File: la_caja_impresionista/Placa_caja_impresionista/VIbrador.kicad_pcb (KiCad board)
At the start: 2 copper layers, 8 parts, among them U1 Pila3,7V, U2 StepDown, U3 Buzzer, U4 HC-05, U5 Buzzer, U6 PiZeroW, U7 Pila3,7V-Modulos-VIbrador-res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

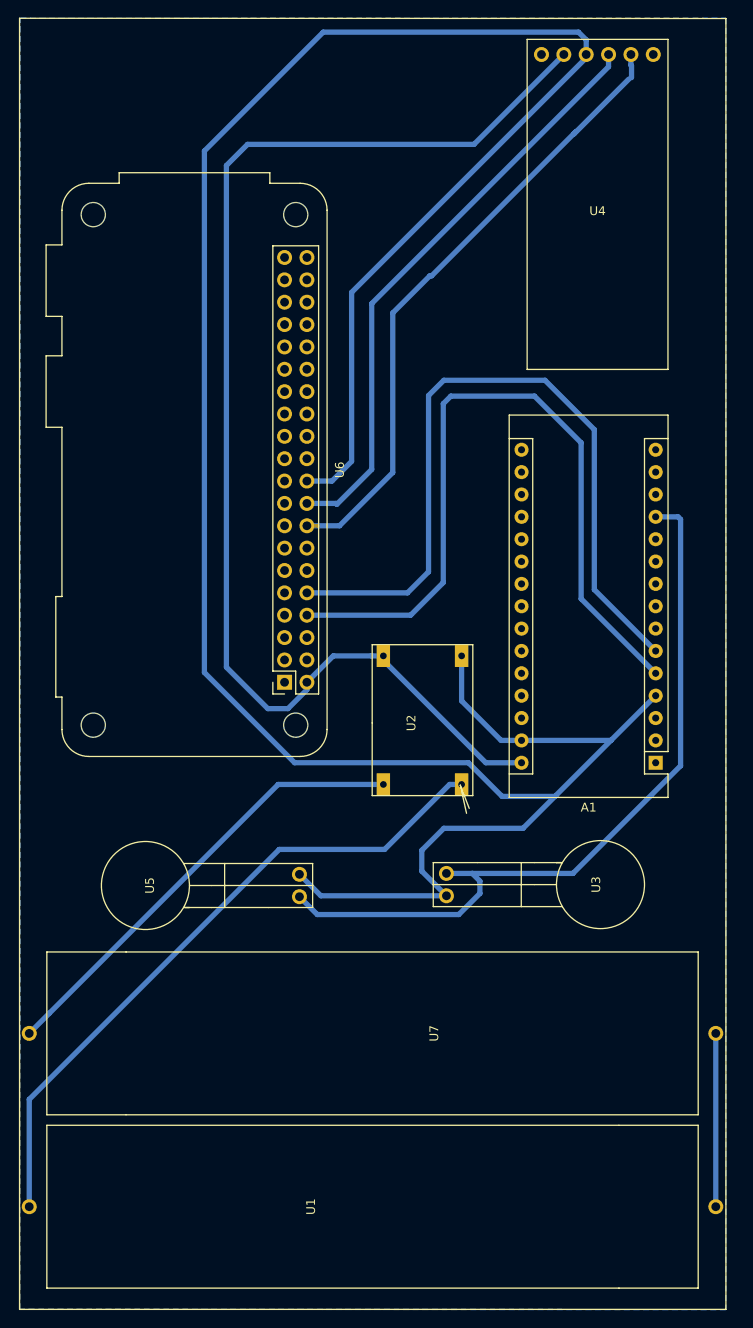
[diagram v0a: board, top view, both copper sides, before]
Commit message: Conexiones PCB
Quedo conectado todo feo y como el orto pero esta conectado que es mejor que nada despues hay que revisar todas las conexiones y dejarlas facheras
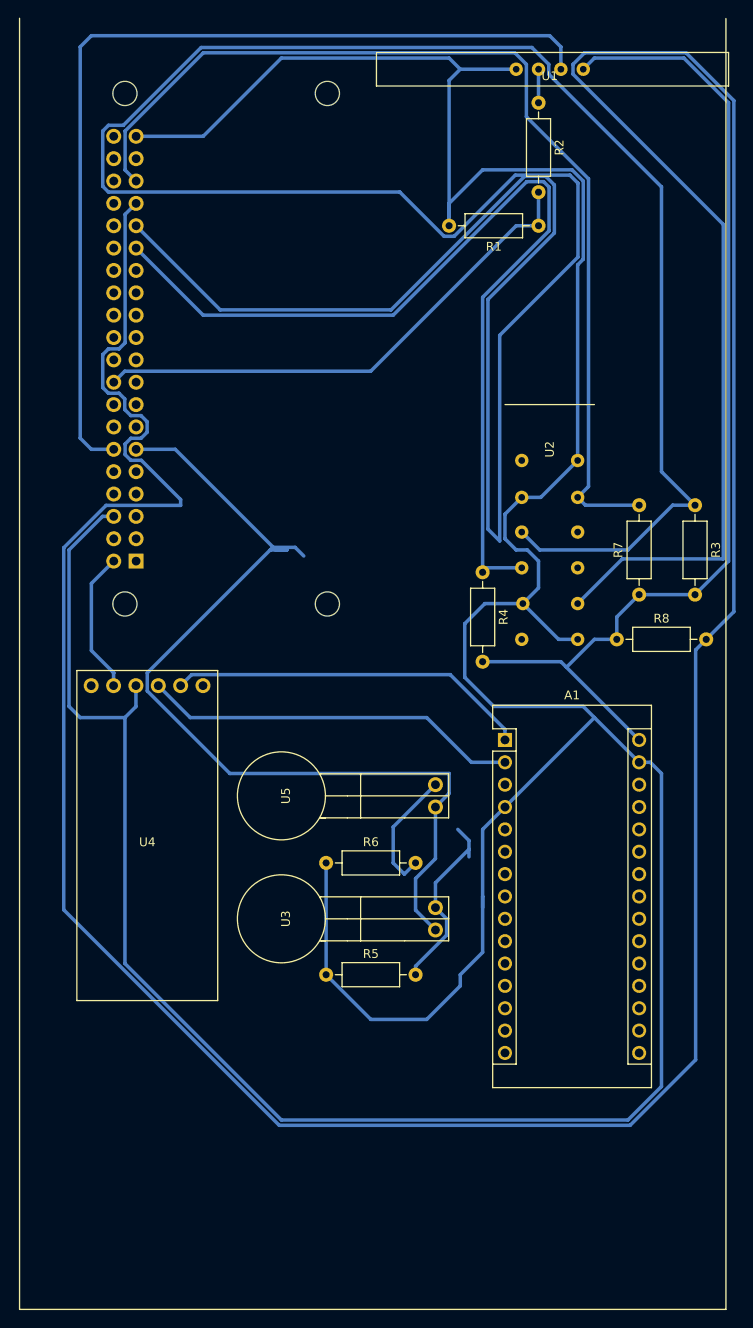
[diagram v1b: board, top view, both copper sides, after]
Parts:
- removed U7: Pila3,7V-Modulos-VIbrador-rescue, VibradorPCB:Pila de Litio
- added R1: 470, devices:R_Axial_DIN0207_L6.3mm_D2.5mm_P10.16mm_Horizontal, F.Cu at (114.3, 72.4)
- added R2: 330, devices:R_Axial_DIN0207_L6.3mm_D2.5mm_P10.16mm_Horizontal, F.Cu at (114.3, 58.4)
- added R3: 10K, devices:R_Axial_DIN0207_L6.3mm_D2.5mm_P10.16mm_Horizontal, F.Cu at (132.1, 104.1)
- added R4: 10K, devices:R_Axial_DIN0207_L6.3mm_D2.5mm_P10.16mm_Horizontal, F.Cu at (108.0, 111.8)
- added R5: 100, devices:R_Axial_DIN0207_L6.3mm_D2.5mm_P10.16mm_Horizontal, F.Cu at (90.2, 157.5)
- added R6: 100, devices:R_Axial_DIN0207_L6.3mm_D2.5mm_P10.16mm_Horizontal, F.Cu at (90.2, 144.8)
- added R7: 10K, devices:R_Axial_DIN0207_L6.3mm_D2.5mm_P10.16mm_Horizontal, F.Cu at (125.7, 114.3)
- added R8: 10K, devices:R_Axial_DIN0207_L6.3mm_D2.5mm_P10.16mm_Horizontal, F.Cu at (123.2, 119.4)
- A1: footprint Module:Arduino_Nano -> Raspberry:Arduino_Nano
- U1: value Pila3,7V -> Ultrasonico; footprint VibradorPCB:Pila de Litio -> VibradorPCB:Ultrasonico
- U2: value StepDown -> Switch-4-posiciones; footprint VibradorPCB:StepDown -> VibradorPCB:Switch_4_posiciones
- U6: footprint Module:Raspberry_Pi_Zero_Socketed_THT_FaceDown_MountingHoles -> Raspberry:Raspberry_Pi_Zero_Socketed_THT_FaceDown_MountingHoles; moved to B.Cu
- moved U1 141.0 mm to (115.6, 55.9), turned to 180 degrees
- moved U4 88.1 mm to (69.8, 121.9)
- moved U3 36.5 mm to (85.1, 151.1), turned to 90 degrees
- moved U2 36.0 mm to (115.6, 99.1), turned to 0 degrees
- moved U6 21.8 mm to (68.6, 110.5), turned to 0 degrees
- moved U5 18.5 mm to (85.1, 137.2)
- moved A1 17.3 mm to (110.5, 130.8), turned to 0 degrees
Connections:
- A1 pad 1: Net-(A1-Pad1) -> RX
- A1 pad 12: D9 -> Net-(A1-Pad12)
- A1 pad 2: Net-(A1-Pad2) -> TX
- A1 pad 29: IN- -> OUT-
- A1 pad 4: IN- -> OUT-
- A1 pad 5: Tx_rasp -> Net-(A1-Pad5)
- A1 pad 6: Rx_rasp -> Net-(A1-Pad6)
- U1 pad 1: Net-(U1-Pad1) -> OUT+
- U1 pad 2: IN- -> TRIG
- U2 pad 1: IN+ -> Net-(U2-Pad1)
- U2 pad 2: OUT+ -> OUT-
- U2 pad 3: IN- -> OUT-
- U2 pad 4: IN- -> SWITCH-4P
- U3 pad 1: D9 -> BUZZER
- U3 pad 2: IN- -> Net-(R5-Pad2)
- U4 pad 3: IN- -> OUT-
- U4 pad 4: RX -> TX
- U4 pad 5: TX -> RX
- U5 pad 1: D9 -> BUZZER
- U5 pad 2: IN- -> Net-(R6-Pad2)
- U6 pad 10: Rx_rasp -> Net-(U6-Pad10)
- U6 pad 11: Net-(U6-Pad11) -> BUZZER
- U6 pad 12: Net-(U6-Pad12) -> TRIG
- U6 pad 16: TX -> Net-(U6-Pad16)
- U6 pad 18: RX -> Net-(R1-Pad1)
- U6 pad 20: IN- -> Net-(U6-Pad20)
- U6 pad 29: Net-(U6-Pad29) -> GPIO5
- U6 pad 31: Net-(U6-Pad31) -> GPIO6
- U6 pad 33: Net-(U6-Pad33) -> SWITCH-10P
- U6 pad 35: Net-(U6-Pad35) -> SWITCH-4P
- U6 pad 39: Net-(U6-Pad39) -> OUT-
- U6 pad 6: Net-(U6-Pad6) -> OUT-
- U6 pad 8: Tx_rasp -> Net-(U6-Pad8)
- U6 pad 9: Net-(U6-Pad9) -> OUT-
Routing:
- net OUT-: track 0.00 -> 428.6 mm
- net SWITCH-10P: track 0.00 -> 400.3 mm
- net IN-: track 377.1 -> 0.00 mm
- net GPIO6: track 0.00 -> 347.5 mm
- net SWITCH-4P: track 0.00 -> 116.0 mm
- net BUZZER: track 0.00 -> 108.4 mm
- net GPIO5: track 0.00 -> 108.2 mm
- net TRIG: track 0.00 -> 107.0 mm
- net D9: track 87.6 -> 0.00 mm
- net Tx_rasp: track 85.3 -> 0.00 mm
- net Rx_rasp: track 84.7 -> 0.00 mm
- net Net-(R1-Pad1): track 0.00 -> 59.4 mm
- net IN+: track 51.9 -> 0.00 mm
- net TX: track 81.3 -> 43.0 mm
- net RX: track 67.3 -> 41.1 mm
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- removed copper zone on B.Cu, net IN-

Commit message: PCB Terminado
Se actualizaron algunos pines de la raspberry ya que al principio se eligio al azar los que iban conectados a el switch y se fue viendo como convenia mas
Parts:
- moved A1 4.44 mm to (108.2, 134.6)
- moved R1 4.44 mm to (112.0, 76.2)
- moved R3 4.44 mm to (129.8, 108.0)
- moved R5 4.44 mm to (87.9, 161.3)
- moved R6 4.44 mm to (87.9, 148.6)
- moved R7 4.44 mm to (123.4, 118.1)
- moved R8 4.44 mm to (120.9, 123.2)
- moved U3 4.44 mm to (82.8, 154.9)
- moved U4 4.44 mm to (67.6, 125.7)
- moved U5 4.44 mm to (82.8, 141.0)
- moved U6 4.44 mm to (66.3, 114.3)
- moved R2 4.44 mm to (112.0, 62.2)
- moved U2 4.44 mm to (113.3, 102.9)
- moved R4 4.44 mm to (105.7, 115.6)
- moved U1 4.44 mm to (113.3, 59.7)
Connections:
- R3 pad 1: GPIO6 -> SWITCH-5P
- U2 pad 5: GPIO6 -> SWITCH-5P
- U6 pad 31: GPIO6 -> Net-(U6-Pad31)
- U6 pad 33: SWITCH-10P -> Net-(U6-Pad33)
- U6 pad 35: SWITCH-4P -> Net-(U6-Pad35)
- U6 pad 38: Net-(U6-Pad38) -> SWITCH-5P
- U6 pad 40: Net-(U6-Pad40) -> SWITCH-4P
- U6 pad 8: Net-(U6-Pad8) -> SWITCH-10P
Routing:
- net GPIO6: track 347.5 -> 0.00 mm
- net SWITCH-5P: track 0.00 -> 144.2 mm
- net SWITCH-10P: track 400.3 -> 358.6 mm
- net BUZZER: track 108.4 -> 97.0 mm
- net Net-(R5-Pad2): track 21.5 -> 11.5 mm
- net GPIO5: track 108.2 -> 115.3 mm
- net OUT-: track 428.6 -> 423.2 mm
- net OUT+: track 133.8 -> 130.2 mm
- net Net-(R6-Pad2): track 14.5 -> 12.2 mm
- net SWITCH-4P: track 116.0 -> 117.2 mm
- net RX: track 41.1 -> 40.4 mm
- added copper zone on B.Cu, net OUT-
